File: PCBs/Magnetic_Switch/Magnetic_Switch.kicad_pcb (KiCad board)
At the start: 2 copper layers, 20 x 25 mm, 2 parts, among them J1 Conn_01x03_Male, U1 SI7201-B-86-IV

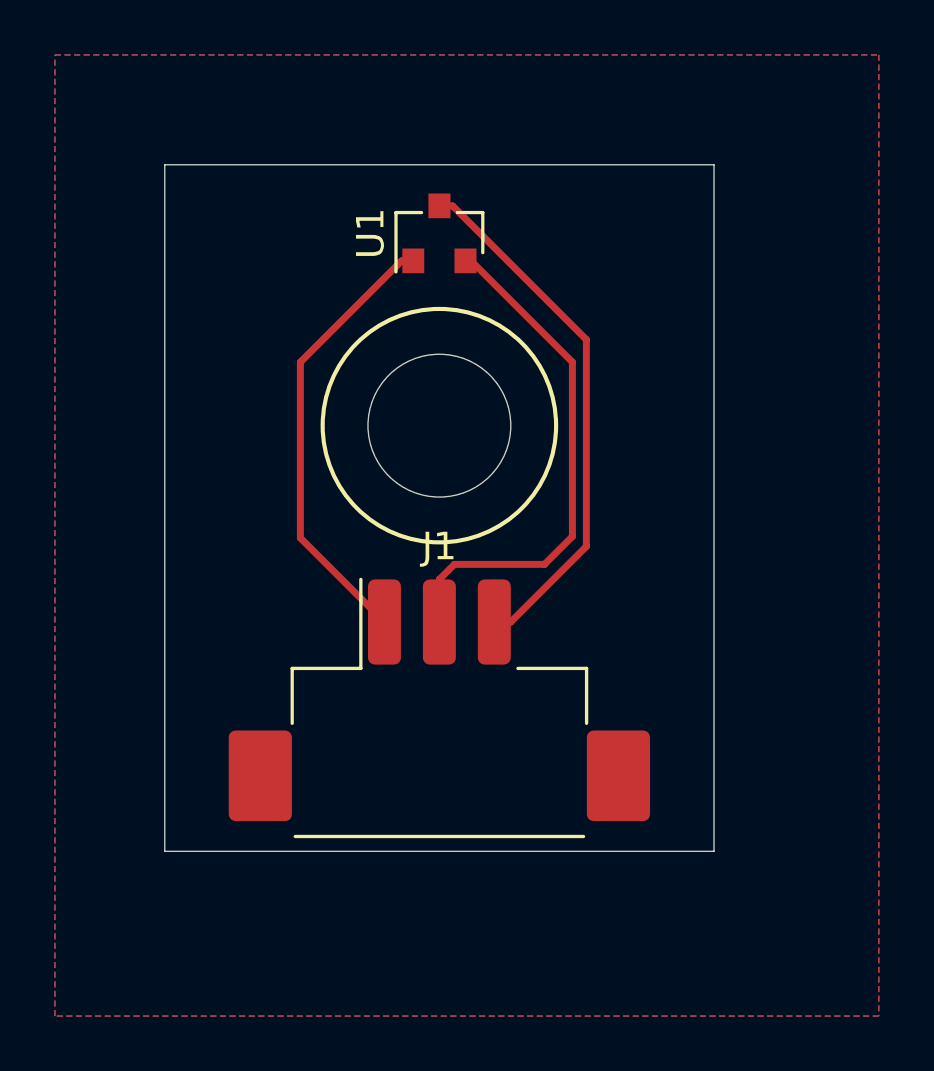
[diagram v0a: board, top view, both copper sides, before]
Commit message: finished magnetic switch
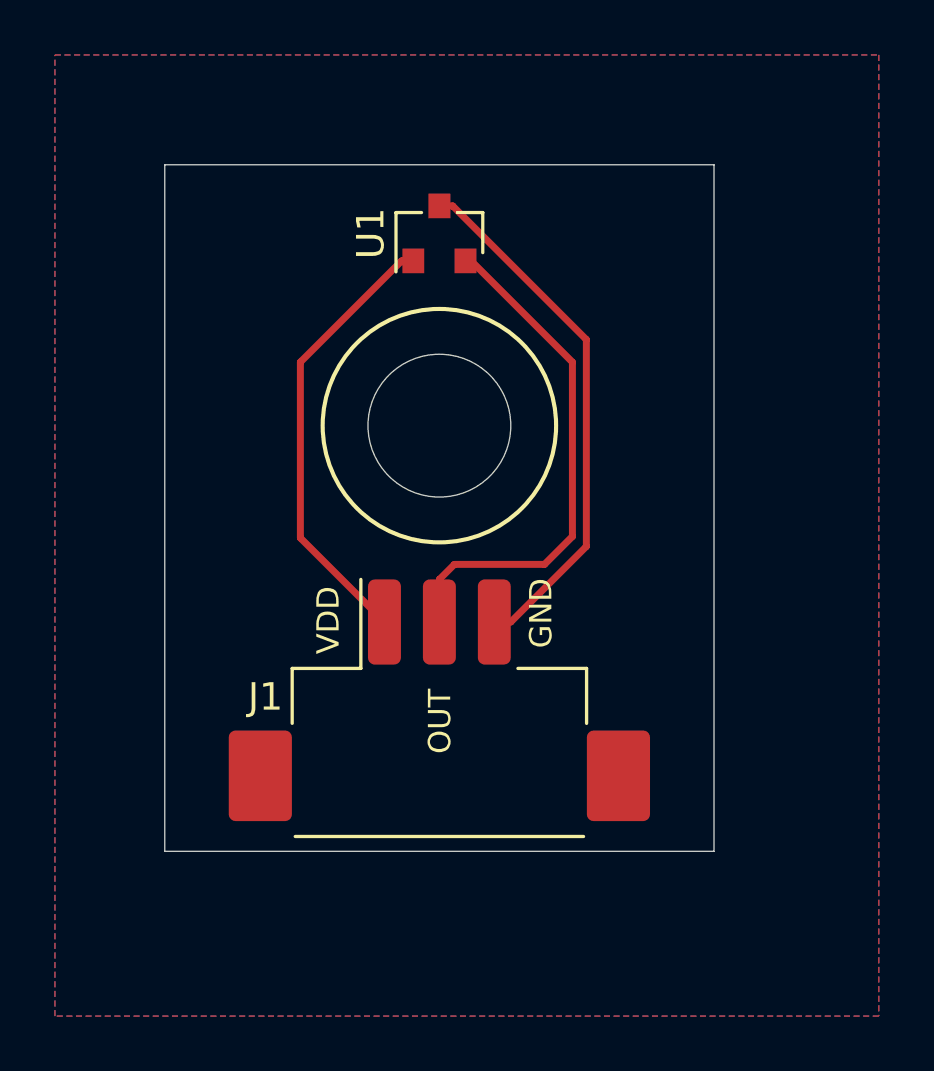
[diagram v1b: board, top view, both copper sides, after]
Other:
- board text added: "GND"
- board text added: "OUT"
- board text added: "VDD"
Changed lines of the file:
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@@
   (general
     (thickness 1.6)
-    (drawings 7)
+    (drawings 10)
     (tracks 16)
     (zones 0)
@@
     (pad_to_mask_clearance 0)
     (aux_axis_origin 0 0)
-    (visible_elements FFFFFF7F)
+    (visible_elements 7FFFFFFF)
     (pcbplotparams
       (layerselection 0x010fc_ffffffff)
@@
       (effects (font (size 1 1) (thickness 0.15)))
     )
+    (fp_line (start 0.76 1.58) (end -0.7 1.58) (layer F.SilkS) (width 0.12))
+    (fp_line (start 0.76 -1.58) (end -1.4 -1.58) (layer F.SilkS) (width 0.12))
+    (fp_line (start -1.7 1.75) (end -1.7 -1.75) (layer F.CrtYd) (width 0.05))
+    (fp_line (start 1.7 1.75) (end -1.7 1.75) (layer F.CrtYd) (width 0.05))
+    (fp_line (start 1.7 -1.75) (end 1.7 1.75) (layer F.CrtYd) (width 0.05))
+    (fp_line (start -1.7 -1.75) (end 1.7 -1.75) (layer F.CrtYd) (width 0.05))
+    (fp_line (start 0.76 -1.58) (end 0.76 -0.65) (layer F.SilkS) (width 0.12))
+    (fp_line (start 0.76 1.58) (end 0.76 0.65) (layer F.SilkS) (width 0.12))
+    (fp_line (start -0.7 1.52) (end 0.7 1.52) (layer F.Fab) (width 0.1))
+    (fp_line (start 0.7 -1.52) (end 0.7 1.52) (layer F.Fab) (width 0.1))
+    (fp_line (start -0.7 -0.95) (end -0.15 -1.52) (layer F.Fab) (width 0.1))
+    (fp_line (start -0.15 -1.52) (end 0.7 -1.52) (layer F.Fab) (width 0.1))
+    (fp_line (start -0.7 -0.95) (end -0.7 1.5) (layer F.Fab) (width 0.1))
     (fp_text user %R (at 0 0) (layer F.Fab)
       (effects (font (size 0.5 0.5) (thickness 0.075)))
     )
-    (fp_line (start -0.7 -0.95) (end -0.7 1.5) (layer F.Fab) (width 0.1))
-    (fp_line (start -0.15 -1.52) (end 0.7 -1.52) (layer F.Fab) (width 0.1))
-    (fp_line (start -0.7 -0.95) (end -0.15 -1.52) (layer F.Fab) (width 0.1))
-    (fp_line (start 0.7 -1.52) (end 0.7 1.52) (layer F.Fab) (width 0.1))
-    (fp_line (start -0.7 1.52) (end 0.7 1.52) (layer F.Fab) (width 0.1))
-    (fp_line (start 0.76 1.58) (end 0.76 0.65) (layer F.SilkS) (width 0.12))
-    (fp_line (start 0.76 -1.58) (end 0.76 -0.65) (layer F.SilkS) (width 0.12))
-    (fp_line (start -1.7 -1.75) (end 1.7 -1.75) (layer F.CrtYd) (width 0.05))
-    (fp_line (start 1.7 -1.75) (end 1.7 1.75) (layer F.CrtYd) (width 0.05))
-    (fp_line (start 1.7 1.75) (end -1.7 1.75) (layer F.CrtYd) (width 0.05))
-    (fp_line (start -1.7 1.75) (end -1.7 -1.75) (layer F.CrtYd) (width 0.05))
-    (fp_line (start 0.76 -1.58) (end -1.4 -1.58) (layer F.SilkS) (width 0.12))
-    (fp_line (start 0.76 1.58) (end -0.7 1.58) (layer F.SilkS) (width 0.12))
     (pad 3 smd rect (at 1 0 90) (size 0.9 0.8) (layers F.Cu F.Paste F.Mask)
       (net 1 "Net-(J1-Pad3)"))
@@
     (tags "connector Hirose  top entry")
     (attr smd)
-    (fp_text reference J1 (at 0 -5.6) (layer F.SilkS)
+    (fp_text reference J1 (at -6.332 -0.122) (layer F.SilkS)
       (effects (font (size 1 1) (thickness 0.15)))
     )
@@
       (effects (font (size 1 1) (thickness 0.15)))
     )
+    (fp_line (start -2 -0.342893) (end -1.5 -1.05) (layer F.Fab) (width 0.1))
+    (fp_line (start -2.5 -1.05) (end -2 -0.342893) (layer F.Fab) (width 0.1))
+    (fp_line (start 8.17 -4.9) (end -8.17 -4.9) (layer F.CrtYd) (width 0.05))
+    (fp_line (start 8.17 5.35) (end 8.17 -4.9) (layer F.CrtYd) (width 0.05))
+    (fp_line (start -8.17 5.35) (end 8.17 5.35) (layer F.CrtYd) (width 0.05))
+    (fp_line (start -8.17 -4.9) (end -8.17 5.35) (layer F.CrtYd) (width 0.05))
+    (fp_line (start 5.25 -1.05) (end 5.25 4.85) (layer F.Fab) (width 0.1))
+    (fp_line (start -5.25 -1.05) (end -5.25 4.85) (layer F.Fab) (width 0.1))
+    (fp_line (start -5.25 4.85) (end 5.25 4.85) (layer F.Fab) (width 0.1))
+    (fp_line (start -5.25 4.96) (end 5.25 4.96) (layer F.SilkS) (width 0.12))
+    (fp_line (start 5.36 -1.16) (end 2.86 -1.16) (layer F.SilkS) (width 0.12))
+    (fp_line (start 5.36 0.84) (end 5.36 -1.16) (layer F.SilkS) (width 0.12))
+    (fp_line (start -2.86 -1.16) (end -2.86 -4.4) (layer F.SilkS) (width 0.12))
+    (fp_line (start -5.36 -1.16) (end -2.86 -1.16) (layer F.SilkS) (width 0.12))
+    (fp_line (start -5.36 0.84) (end -5.36 -1.16) (layer F.SilkS) (width 0.12))
+    (fp_line (start -5.25 -1.05) (end 5.25 -1.05) (layer F.Fab) (width 0.1))
     (fp_text user %R (at 0 1.9) (layer F.Fab)
       (effects (font (size 1 1) (thickness 0.15)))
     )
-    (fp_line (start -5.25 -1.05) (end 5.25 -1.05) (layer F.Fab) (width 0.1))
-    (fp_line (start -5.36 0.84) (end -5.36 -1.16) (layer F.SilkS) (width 0.12))
-    (fp_line (start -5.36 -1.16) (end -2.86 -1.16) (layer F.SilkS) (width 0.12))
-    (fp_line (start -2.86 -1.16) (end -2.86 -4.4) (layer F.SilkS) (width 0.12))
-    (fp_line (start 5.36 0.84) (end 5.36 -1.16) (layer F.SilkS) (width 0.12))
-    (fp_line (start 5.36 -1.16) (end 2.86 -1.16) (layer F.SilkS) (width 0.12))
-    (fp_line (start -5.25 4.96) (end 5.25 4.96) (layer F.SilkS) (width 0.12))
-    (fp_line (start -5.25 4.85) (end 5.25 4.85) (layer F.Fab) (width 0.1))
-    (fp_line (start -5.25 -1.05) (end -5.25 4.85) (layer F.Fab) (width 0.1))
-    (fp_line (start 5.25 -1.05) (end 5.25 4.85) (layer F.Fab) (width 0.1))
-    (fp_line (start -8.17 -4.9) (end -8.17 5.35) (layer F.CrtYd) (width 0.05))
-    (fp_line (start -8.17 5.35) (end 8.17 5.35) (layer F.CrtYd) (width 0.05))
-    (fp_line (start 8.17 5.35) (end 8.17 -4.9) (layer F.CrtYd) (width 0.05))
-    (fp_line (start 8.17 -4.9) (end -8.17 -4.9) (layer F.CrtYd) (width 0.05))
-    (fp_line (start -2.5 -1.05) (end -2 -0.342893) (layer F.Fab) (width 0.1))
-    (fp_line (start -2 -0.342893) (end -1.5 -1.05) (layer F.Fab) (width 0.1))
     (pad MP smd roundrect (at 6.52 2.75) (size 2.3 3.3) (layers F.Cu F.Paste F.Mask) (roundrect_rratio 0.108696))
     (pad MP smd roundrect (at -6.52 2.75) (size 2.3 3.3) (layers F.Cu F.Paste F.Mask) (roundrect_rratio 0.108696))
@@
     )
   )
+  (gr_text GND (at 147.701 100.33 90) (layer F.SilkS)
+    (effects (font (size 0.8128 0.8128) (thickness 0.1524)))
+  )
+  (gr_text OUT (at 144.018 104.267 90) (layer F.SilkS)
+    (effects (font (size 0.8128 0.8128) (thickness 0.1524)))
+  )
+  (gr_text VDD (at 139.954 100.584 90) (layer F.SilkS)
+    (effects (font (size 0.8128 0.8128) (thickness 0.1524)))
+  )
   (gr_line (start 144 84) (end 144 109) (layer Dwgs.User) (width 0.15))

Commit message: gerber files
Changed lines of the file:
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@@
     (pcbplotparams
       (layerselection 0x010fc_ffffffff)
-      (usegerberextensions false)
-      (usegerberattributes true)
-      (usegerberadvancedattributes true)
-      (creategerberjobfile true)
+      (usegerberextensions true)
+      (usegerberattributes false)
+      (usegerberadvancedattributes false)
+      (creategerberjobfile false)
       (excludeedgelayer true)
       (linewidth 0.100000)
@@
       (psa4output false)
       (plotreference true)
-      (plotvalue true)
+      (plotvalue false)
       (plotinvisibletext false)
       (padsonsilk false)
-      (subtractmaskfromsilk false)
+      (subtractmaskfromsilk true)
       (outputformat 1)
       (mirror false)
-      (drillshape 1)
+      (drillshape 0)
       (scaleselection 1)
-      (outputdirectory ""))
+      (outputdirectory "./Output"))
   )
   (net 0 "")
@@
       (effects (font (size 1 1) (thickness 0.15)))
     )
+    (fp_line (start -0.7 -0.95) (end -0.7 1.5) (layer F.Fab) (width 0.1))
+    (fp_line (start -0.15 -1.52) (end 0.7 -1.52) (layer F.Fab) (width 0.1))
+    (fp_line (start -0.7 -0.95) (end -0.15 -1.52) (layer F.Fab) (width 0.1))
+    (fp_line (start 0.7 -1.52) (end 0.7 1.52) (layer F.Fab) (width 0.1))
+    (fp_line (start -0.7 1.52) (end 0.7 1.52) (layer F.Fab) (width 0.1))
+    (fp_line (start 0.76 1.58) (end 0.76 0.65) (layer F.SilkS) (width 0.12))
+    (fp_line (start 0.76 -1.58) (end 0.76 -0.65) (layer F.SilkS) (width 0.12))
+    (fp_line (start -1.7 -1.75) (end 1.7 -1.75) (layer F.CrtYd) (width 0.05))
+    (fp_line (start 1.7 -1.75) (end 1.7 1.75) (layer F.CrtYd) (width 0.05))
+    (fp_line (start 1.7 1.75) (end -1.7 1.75) (layer F.CrtYd) (width 0.05))
+    (fp_line (start -1.7 1.75) (end -1.7 -1.75) (layer F.CrtYd) (width 0.05))
+    (fp_line (start 0.76 -1.58) (end -1.4 -1.58) (layer F.SilkS) (width 0.12))
     (fp_line (start 0.76 1.58) (end -0.7 1.58) (layer F.SilkS) (width 0.12))
-    (fp_line (start 0.76 -1.58) (end -1.4 -1.58) (layer F.SilkS) (width 0.12))
-    (fp_line (start -1.7 1.75) (end -1.7 -1.75) (layer F.CrtYd) (width 0.05))
-    (fp_line (start 1.7 1.75) (end -1.7 1.75) (layer F.CrtYd) (width 0.05))
-    (fp_line (start 1.7 -1.75) (end 1.7 1.75) (layer F.CrtYd) (width 0.05))
-    (fp_line (start -1.7 -1.75) (end 1.7 -1.75) (layer F.CrtYd) (width 0.05))
-    (fp_line (start 0.76 -1.58) (end 0.76 -0.65) (layer F.SilkS) (width 0.12))
-    (fp_line (start 0.76 1.58) (end 0.76 0.65) (layer F.SilkS) (width 0.12))
-    (fp_line (start -0.7 1.52) (end 0.7 1.52) (layer F.Fab) (width 0.1))
-    (fp_line (start 0.7 -1.52) (end 0.7 1.52) (layer F.Fab) (width 0.1))
-    (fp_line (start -0.7 -0.95) (end -0.15 -1.52) (layer F.Fab) (width 0.1))
-    (fp_line (start -0.15 -1.52) (end 0.7 -1.52) (layer F.Fab) (width 0.1))
-    (fp_line (start -0.7 -0.95) (end -0.7 1.5) (layer F.Fab) (width 0.1))
     (fp_text user %R (at 0 0) (layer F.Fab)
       (effects (font (size 0.5 0.5) (thickness 0.075)))
@@
       (effects (font (size 1 1) (thickness 0.15)))
     )
+    (fp_line (start -5.25 -1.05) (end 5.25 -1.05) (layer F.Fab) (width 0.1))
+    (fp_line (start -5.36 0.84) (end -5.36 -1.16) (layer F.SilkS) (width 0.12))
+    (fp_line (start -5.36 -1.16) (end -2.86 -1.16) (layer F.SilkS) (width 0.12))
+    (fp_line (start -2.86 -1.16) (end -2.86 -4.4) (layer F.SilkS) (width 0.12))
+    (fp_line (start 5.36 0.84) (end 5.36 -1.16) (layer F.SilkS) (width 0.12))
+    (fp_line (start 5.36 -1.16) (end 2.86 -1.16) (layer F.SilkS) (width 0.12))
+    (fp_line (start -5.25 4.96) (end 5.25 4.96) (layer F.SilkS) (width 0.12))
+    (fp_line (start -5.25 4.85) (end 5.25 4.85) (layer F.Fab) (width 0.1))
+    (fp_line (start -5.25 -1.05) (end -5.25 4.85) (layer F.Fab) (width 0.1))
+    (fp_line (start 5.25 -1.05) (end 5.25 4.85) (layer F.Fab) (width 0.1))
+    (fp_line (start -8.17 -4.9) (end -8.17 5.35) (layer F.CrtYd) (width 0.05))
+    (fp_line (start -8.17 5.35) (end 8.17 5.35) (layer F.CrtYd) (width 0.05))
+    (fp_line (start 8.17 5.35) (end 8.17 -4.9) (layer F.CrtYd) (width 0.05))
+    (fp_line (start 8.17 -4.9) (end -8.17 -4.9) (layer F.CrtYd) (width 0.05))
+    (fp_line (start -2.5 -1.05) (end -2 -0.342893) (layer F.Fab) (width 0.1))
     (fp_line (start -2 -0.342893) (end -1.5 -1.05) (layer F.Fab) (width 0.1))
-    (fp_line (start -2.5 -1.05) (end -2 -0.342893) (layer F.Fab) (width 0.1))
-    (fp_line (start 8.17 -4.9) (end -8.17 -4.9) (layer F.CrtYd) (width 0.05))
-    (fp_line (start 8.17 5.35) (end 8.17 -4.9) (layer F.CrtYd) (width 0.05))
-    (fp_line (start -8.17 5.35) (end 8.17 5.35) (layer F.CrtYd) (width 0.05))
-    (fp_line (start -8.17 -4.9) (end -8.17 5.35) (layer F.CrtYd) (width 0.05))
-    (fp_line (start 5.25 -1.05) (end 5.25 4.85) (layer F.Fab) (width 0.1))
-    (fp_line (start -5.25 -1.05) (end -5.25 4.85) (layer F.Fab) (width 0.1))
-    (fp_line (start -5.25 4.85) (end 5.25 4.85) (layer F.Fab) (width 0.1))
-    (fp_line (start -5.25 4.96) (end 5.25 4.96) (layer F.SilkS) (width 0.12))
-    (fp_line (start 5.36 -1.16) (end 2.86 -1.16) (layer F.SilkS) (width 0.12))
-    (fp_line (start 5.36 0.84) (end 5.36 -1.16) (layer F.SilkS) (width 0.12))
-    (fp_line (start -2.86 -1.16) (end -2.86 -4.4) (layer F.SilkS) (width 0.12))
-    (fp_line (start -5.36 -1.16) (end -2.86 -1.16) (layer F.SilkS) (width 0.12))
-    (fp_line (start -5.36 0.84) (end -5.36 -1.16) (layer F.SilkS) (width 0.12))
-    (fp_line (start -5.25 -1.05) (end 5.25 -1.05) (layer F.Fab) (width 0.1))
     (fp_text user %R (at 0 1.9) (layer F.Fab)
       (effects (font (size 1 1) (thickness 0.15)))
     )
-    (pad MP smd roundrect (at 6.52 2.75) (size 2.3 3.3) (layers F.Cu F.Paste F.Mask) (roundrect_rratio 0.108696))
-    (pad MP smd roundrect (at -6.52 2.75) (size 2.3 3.3) (layers F.Cu F.Paste F.Mask) (roundrect_rratio 0.108696))
-    (pad 3 smd roundrect (at 2 -2.85) (size 1.2 3.1) (layers F.Cu F.Paste F.Mask) (roundrect_rratio 0.208333)
+    (pad MP smd roundrect (at 6.52 2.75) (size 2.3 3.3) (layers F.Cu F.Paste F.Mask) (roundrect_rratio 0.108695652173913))
+    (pad MP smd roundrect (at -6.52 2.75) (size 2.3 3.3) (layers F.Cu F.Paste F.Mask) (roundrect_rratio 0.108695652173913))
+    (pad 3 smd roundrect (at 2 -2.85) (size 1.2 3.1) (layers F.Cu F.Paste F.Mask) (roundrect_rratio 0.2083325)
       (net 1 "Net-(J1-Pad3)"))
-    (pad 2 smd roundrect (at 0 -2.85) (size 1.2 3.1) (layers F.Cu F.Paste F.Mask) (roundrect_rratio 0.208333)
+    (pad 2 smd roundrect (at 0 -2.85) (size 1.2 3.1) (layers F.Cu F.Paste F.Mask) (roundrect_rratio 0.2083325)
       (net 2 "Net-(J1-Pad2)"))
-    (pad 1 smd roundrect (at -2 -2.85) (size 1.2 3.1) (layers F.Cu F.Paste F.Mask) (roundrect_rratio 0.208333)
+    (pad 1 smd roundrect (at -2 -2.85) (size 1.2 3.1) (layers F.Cu F.Paste F.Mask) (roundrect_rratio 0.2083325)
       (net 3 "Net-(J1-Pad1)"))
     (model ${KISYS3DMOD}/Connector_Hirose.3dshapes/Hirose_DF3EA-03P-2H_1x03-1MP_P2.00mm_Horizontal.wrl

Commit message: th
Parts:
- J1: footprint Connector_Hirose:Hirose_DF3EA-03P-2H_1x03-1MP_P2.00mm_Horizontal -> Connector_PinHeader_2.54mm:PinHeader_1x03_P2.54mm_Vertical
- moved J1 2.54 mm to (144.0, 101.0)
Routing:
- net Net-(J1-Pad3): track 19.4 -> 25.7 mm
- net Net-(J1-Pad1): track 16.4 -> 18.8 mm
- net Net-(J1-Pad2): track 18.8 -> 20.8 mm
- added copper zone on B.Cu, net Net-(J1-Pad3)
- removed copper zone on B.Cu, net (none)
